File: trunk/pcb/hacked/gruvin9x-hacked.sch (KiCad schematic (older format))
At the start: 156 parts, among them K1 CONN_3, P1 CONN_5X2, P2 CONN_5, P3 CONN_6, P4 CONN_9, P5 CONN_9, P6 CONN_6, P7 CONN_12, P8 CONN_30, Q1 2SC9014, Q2 BC847C, Q3 BC857C, SW1 SW_PUSH, SW2 SW_PUSH, SW3 SW_PUSH, SW4 SW_PUSH, SW5 SW_PUSH, SW6 SW_PUSH, U1 78L05, U2 4066, U3 LN-6206-30, X1 16MHz

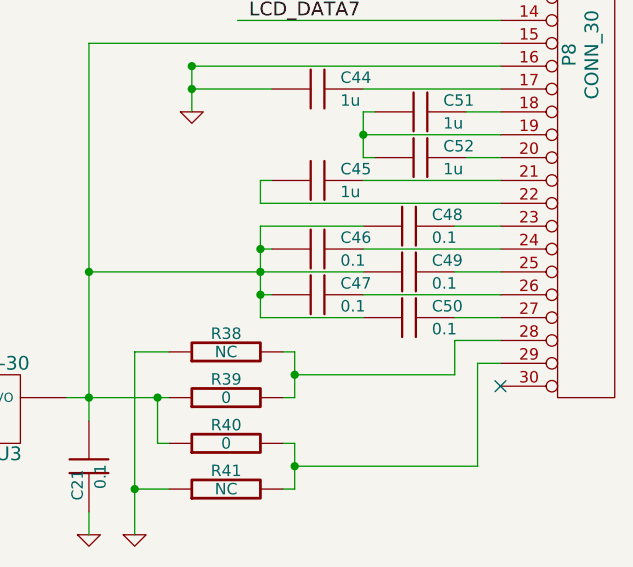
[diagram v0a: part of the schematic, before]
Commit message: PCB V3 re-routed to corrected V3 schematic (trims + PPM-in inverting buffer). Corrections made to LCD decoupling capacitor values (1uF) on other schematics.
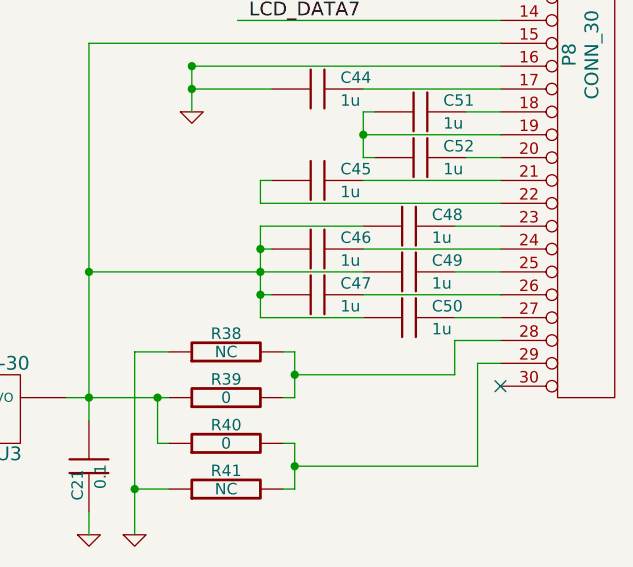
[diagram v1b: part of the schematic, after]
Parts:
- C46, C47, C48, C49, C50: value 0.1 -> 1u
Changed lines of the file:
@@
-EESchema Schematic File Version 2  date 28/12/2010 12:05:06 p.m.
+EESchema Schematic File Version 2  date 14/01/2011 12:24:02 p.m.
 LIBS:power
 LIBS:device
@@
 Sheet 1 1
 Title "Main Controller PCB (Stock)"
-Date "27 dec 2010"
-Rev "1.2"
+Date "13 jan 2011"
+Rev "1.3"
 Comp "gruvin9x"
 Comment1 "(Layout designed to suit easy conversion to 2xA4 if required.)"
@@
 P 14700 3600
 F 0 "C50" V 14650 3700 50  0000 L CNN
-F 1 "0.1" V 14750 3700 50  0000 L CNN
+F 1 "1u" V 14750 3700 50  0000 L CNN
 	1    14700 3600
 	0    1    1    0
@@
 P 14300 3500
 F 0 "C47" V 14250 3600 50  0000 L CNN
-F 1 "0.1" V 14350 3600 50  0000 L CNN
+F 1 "1u" V 14350 3600 50  0000 L CNN
 	1    14300 3500
 	0    1    1    0
@@
 P 14300 3300
 F 0 "C46" V 14250 3400 50  0000 L CNN
-F 1 "0.1" V 14350 3400 50  0000 L CNN
+F 1 "1u" V 14350 3400 50  0000 L CNN
 	1    14300 3300
 	0    1    1    0
@@
 P 14700 3400
 F 0 "C49" V 14650 3500 50  0000 L CNN
-F 1 "0.1" V 14750 3500 50  0000 L CNN
+F 1 "1u" V 14750 3500 50  0000 L CNN
 	1    14700 3400
 	0    1    1    0
@@
 P 14700 3200
 F 0 "C48" V 14650 3300 50  0000 L CNN
-F 1 "0.1" V 14750 3300 50  0000 L CNN
+F 1 "1u" V 14750 3300 50  0000 L CNN
 	1    14700 3200
 	0    1    1    0
